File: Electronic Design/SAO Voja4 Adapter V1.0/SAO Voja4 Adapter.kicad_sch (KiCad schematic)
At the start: 37 parts, among them J1 Conn_01x12_Socket, J2 BATTERY, Q1 MMBT4401LT1G, Q2 MMBT4401LT1G, Q3 MMBT4401LT1G, Q4 MMBT4401LT1G, U1 SSP9193-33M5R, X1 SAO_conn, X2 Header_11-PIN_0.1, X3 HEADER_11-PIN_0.1, X4 QWIIC

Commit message: Released V1 boards
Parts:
- X2: value Header_11-PIN_0.1 -> Header_9-PIN_0.1; footprint Connector_PinSocket_2.54mm:PinSocket_1x11_P2.54mm_Vertical -> Connector_PinSocket_2.54mm:PinSocket_1x09_P2.54mm_Vertical; symbol Connector_Generic:Conn_01x11 -> Connector_Generic:Conn_01x09
- renumbered JP3 to JP2, JP4 to JP3, JP2 to JP4, R5 to R1, R1 to R2, R2 to R3, R6 to R5, R7 to R6
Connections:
- net QSPI_D1 is gone; now on net SPI_SDO: X2.5 (Pin_5)
- net QSPI_D2 is gone; now on net SPI_CS1: X2.4 (Pin_4)
- net GND: now also X2.8 (Pin_8); no longer X2.10 (Pin_10)
- net OUT0: no longer JP2.2 (B), R1.2
- net OUT1: no longer JP4.2 (B), R4.2
- net SPI_CD: now also X2.1 (Pin_1); no longer X2.3 (Pin_3)
- net SPI_CLK: now also X2.7 (Pin_7); no longer X2.9 (Pin_9)
- net SPI_CS1: no longer JP11.2 (B), JP30.2 (C), X2.6 (Pin_6)
- net SPI_CS2: no longer X2.1 (Pin_1)
- net SPI_RST: no longer X2.2 (Pin_2)
- net SPI_SDI: now also X2.6 (Pin_6); no longer X2.8 (Pin_8)
- net SPI_SDO: no longer X2.7 (Pin_7)
- net VIN: now also X2.9 (Pin_9); no longer X2.11 (Pin_11)
- new net SPI_CS: JP11.2 (B), JP30.2 (C)
- new net jOUT0: JP2.2 (B), R1.2
- new net jOUT1: JP4.2 (B), R4.2
- no-connect marks 11 -> 9

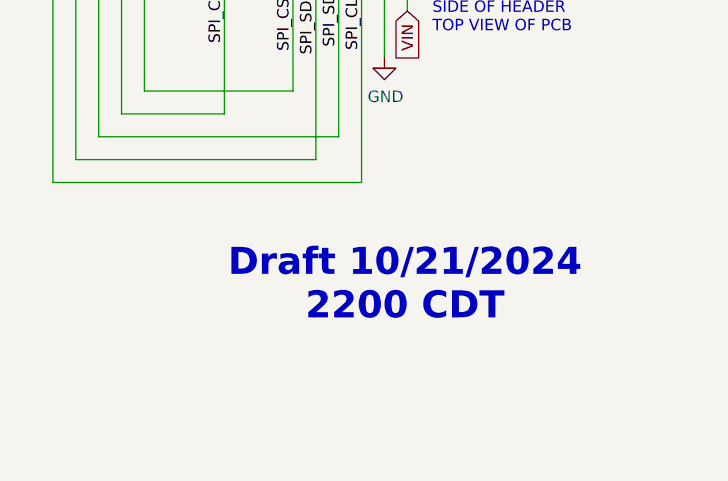
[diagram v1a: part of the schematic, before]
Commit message: Remove draft V1 schematic
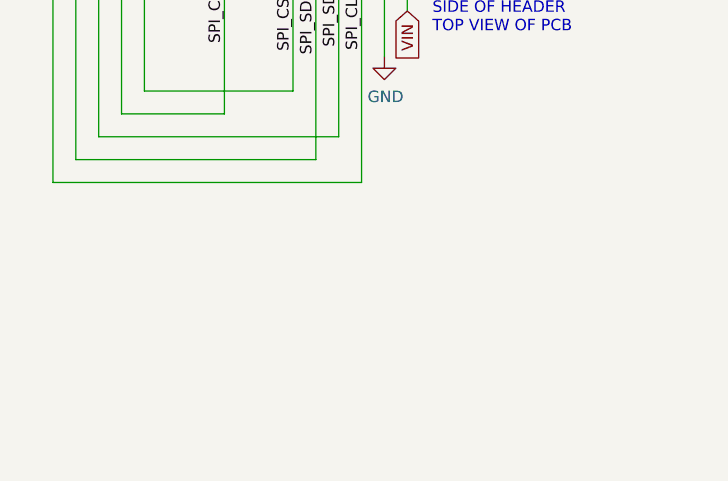
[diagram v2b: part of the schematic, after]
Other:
- note removed: "Draft 10/21/2024 2200 CDT"
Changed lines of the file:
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@@
-		)
-	)
-	(text "Draft 10/21/2024\n2200 CDT"
-		(exclude_from_sim no)
-		(at 243.586 181.61 0)
-		(effects
-			(font
-				(size 3 3)
-				(thickness 0.6)
-				(bold yes)
-				(color 255 13 6 1)
-			)
 		)
 	)

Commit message: Add BOM items in KiCAD schematic
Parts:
- C1, C3: Manufacturer (none) -> Samsung; Manufacturer_Part_Number (none) -> CL21B105KAFNNNE
- C2: Manufacturer (none) -> Samsung; Manufacturer_Part_Number (none) -> CL21B103KBANNNC
- J1: Manufacturer (none) -> Sullins; Manufacturer_Part_Number (none) -> PPTC121LGBN-RC
- Q1, Q2, Q3, Q4: Manufacturer_Part_Number (none) -> MMBT4401LT1G
- R1, R4: Manufacturer (none) -> KOA SPEER; Manufacturer_Part_Number (none) -> RK73H2ATTD4700F
- R2, R3, R5, R6: Manufacturer (none) -> KOA SPEER; Manufacturer_Part_Number (none) -> RK73H2ATTD3301F
- U1: Manufacturer (none) -> TI; Manufacturer_Part_Number SGM2007-3.3XN5/TR -> TLV75533PDBVR
- X1: Manufacturer (none) -> Sullins; Manufacturer_Part_Number (none) -> SFH11-NBPC-D03-ST-BK
- X4: Manufacturer_Part_Number (none) -> SM04B-SRSS-TB
